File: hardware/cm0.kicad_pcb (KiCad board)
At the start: 4 copper layers, 3 parts, among them U1 H3, U2 H5TQ4G63EFR, U3 H5TQ4G63EFR

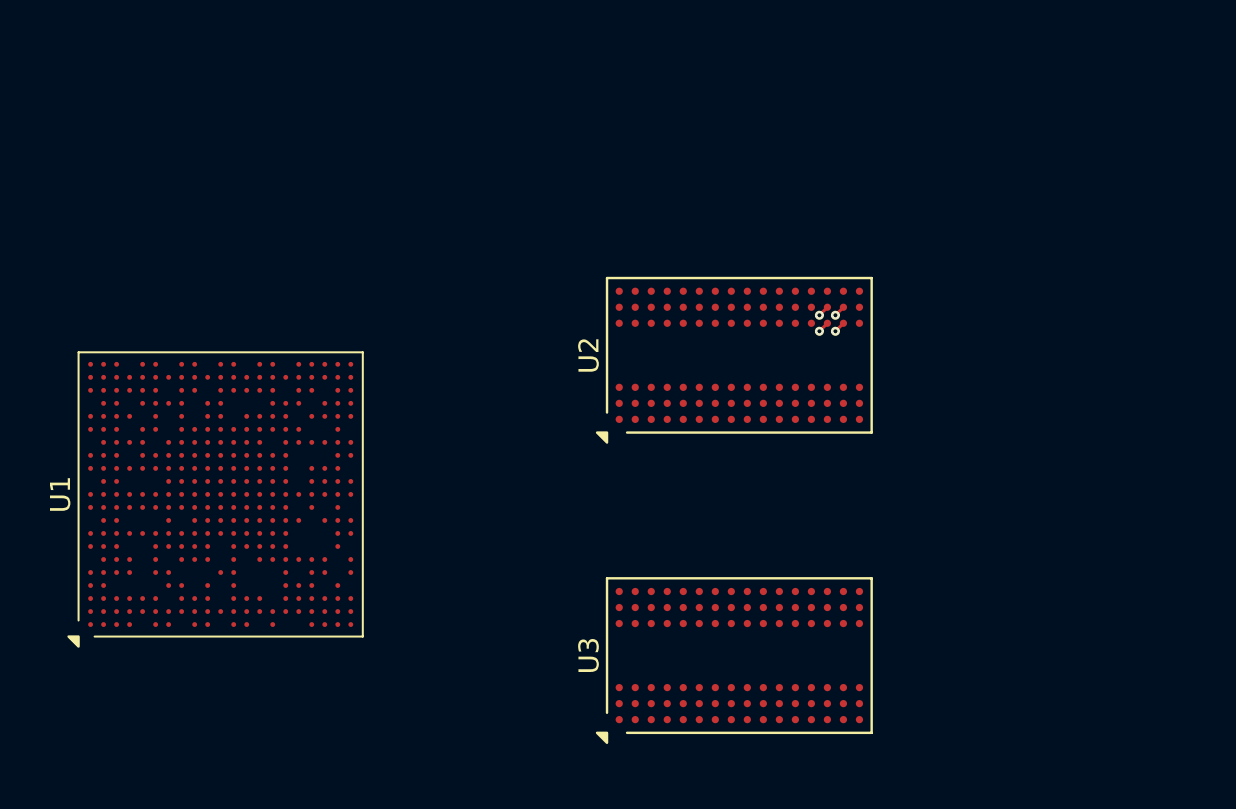
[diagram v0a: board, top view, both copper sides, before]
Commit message: Routed DDR3
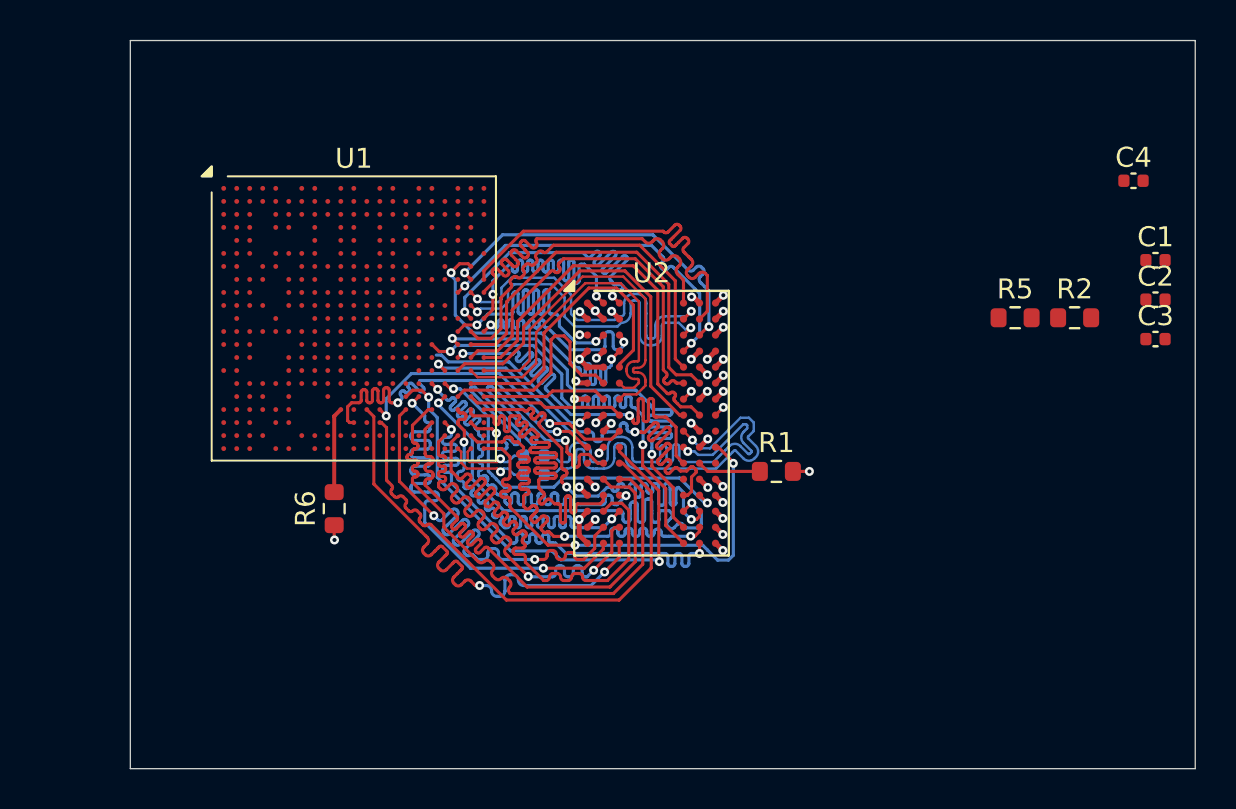
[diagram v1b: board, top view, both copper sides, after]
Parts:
- removed U3: H5TQ4G63EFR, Package_BGA:FBGA-96_7.5x13mm_Layout9x16_P0.8mm
- added C1: 100nF, Capacitor_SMD:C_0402_1005Metric, F.Cu at (135.7, 102.2)
- added C2: 100nF, Capacitor_SMD:C_0402_1005Metric, F.Cu at (135.7, 104.1)
- added C3: 100nF, Capacitor_SMD:C_0402_1005Metric, F.Cu at (135.7, 106.1)
- added C4: 100nF, Capacitor_SMD:C_0402_1005Metric, F.Cu at (134.6, 98.2)
- added R1: 243, Resistor_SMD:R_0603_1608Metric, F.Cu at (116.8, 112.7)
- added R2: 2k, Resistor_SMD:R_0603_1608Metric, F.Cu at (131.7, 105.0)
- added R3: 22, Resistor_SMD:R_0402_1005Metric, B.Cu at (104.6, 112.9)
- added R4: 22, Resistor_SMD:R_0402_1005Metric, B.Cu at (104.6, 111.9)
- added R5: 2k, Resistor_SMD:R_0603_1608Metric, F.Cu at (128.7, 105.0)
- added R6: 243, Resistor_SMD:R_0603_1608Metric, F.Cu at (94.7, 114.6)
- moved U1 11.0 mm to (95.6, 105.1), turned to 0 degrees
- moved U2 5.55 mm to (110.5, 110.3), turned to 0 degrees
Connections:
- net /DDR3/DQS0 renamed /DDR3/DQS0+
- net /DDR3/DQS1 renamed /DDR3/DQS1+
- net /DDR3/~{DQS0} renamed /DDR3/DQS0-
- net /DDR3/~{DQS1} renamed /DDR3/DQS1-
- U1 pad AA15: /DDR3/DQS2 -> /DDR3/DQS2+
- U1 pad AA19: Net-(U1-SCK) -> /H3/C+
- U1 pad AA20: Net-(U1-SCKB) -> /H3/C-
- U1 pad AA9: /DDR3/DQS3 -> /DDR3/DQS3+
- U1 pad H20: /DDR3/DQ9 -> /DDR3/DQ10
- U1 pad H21: /DDR3/DQ10 -> /DDR3/DQ14
- U1 pad J21: /DDR3/DQ11 -> /DDR3/DQ12
- U1 pad L20: /DDR3/DQ12 -> /DDR3/DQ15
- U1 pad M19: /DDR3/DQ15 -> /DDR3/DQ11
- U1 pad M21: /DDR3/DQ14 -> /DDR3/DQ9
- U1 pad N20: /DDR3/DQ0 -> /DDR3/DQ3
- U1 pad P20: /DDR3/DQ2 -> /DDR3/DQ1
- U1 pad P21: /DDR3/DQ1 -> /DDR3/DQ5
- U1 pad R19: /DDR3/DQ4 -> /DDR3/DQ7
- U1 pad T16: unconnected-(U1-SVREF-PadT16) -> VREF
- U1 pad T20: /DDR3/DQ5 -> /DDR3/DQ0
- U1 pad U19: /DDR3/DQ6 -> /DDR3/DQ2
- U1 pad U20: /DDR3/DQ7 -> /DDR3/DQ4
- U1 pad U21: /DDR3/DQ3 -> /DDR3/DQ6
- U1 pad V10: unconnected-(U1-SZQ-PadV10) -> Net-(U1-SZQ)
- U1 pad Y15: /DDR3/~{DQS2} -> /DDR3/DQS2-
- U1 pad Y9: /DDR3/~{DQS3} -> /DDR3/DQS3-
- U2 pad H1: /DDR3/VREF -> VREF
- U2 pad M8: /DDR3/VREF -> VREF
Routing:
- net /DDR3/BA0: track 0.00 -> 26.4 mm
- net /DDR3/~{WE}: track 0.00 -> 26.4 mm
- net /DDR3/BA2: track 0.00 -> 26.3 mm
- net /DDR3/A3: track 0.00 -> 26.3 mm
- net /DDR3/A5: track 0.00 -> 26.3 mm
- net /DDR3/~{CAS}: track 0.00 -> 25.0 mm, vias 0 -> 2
- net /DDR3/~{CS}: track 0.00 -> 24.9 mm, vias 0 -> 2
- net /DDR3/A14: track 0.00 -> 24.9 mm, vias 0 -> 2
- net /DDR3/~{RESET}: track 0.00 -> 24.9 mm, vias 0 -> 2
- net /DDR3/A10: track 0.00 -> 24.8 mm, vias 0 -> 2
- net /DDR3/A12: track 0.00 -> 24.8 mm, vias 0 -> 2
- net /DDR3/A13: track 0.00 -> 24.8 mm, vias 0 -> 2
- net /DDR3/A7: track 0.00 -> 24.8 mm, vias 0 -> 2
- net /DDR3/A8: track 0.00 -> 24.8 mm, vias 0 -> 2
- net /DDR3/A0: track 0.00 -> 24.7 mm, vias 0 -> 2
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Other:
- board outline added: 53.2 x 36.4 mm
